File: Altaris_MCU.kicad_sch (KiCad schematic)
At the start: 82 parts, among them J1 Screw_Terminal_01x02, J10 USB_C_Receptacle_USB2.0_16P, J11 Screw_Terminal_01x02, J12 Screw_Terminal_01x02, J2 Screw_Terminal_01x02, J3 Screw_Terminal_01x02, J4 Screw_Terminal_01x02, J5 Screw_Terminal_01x02, J6 Screw_Terminal_01x02, J7 Conn_01x08_Socket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

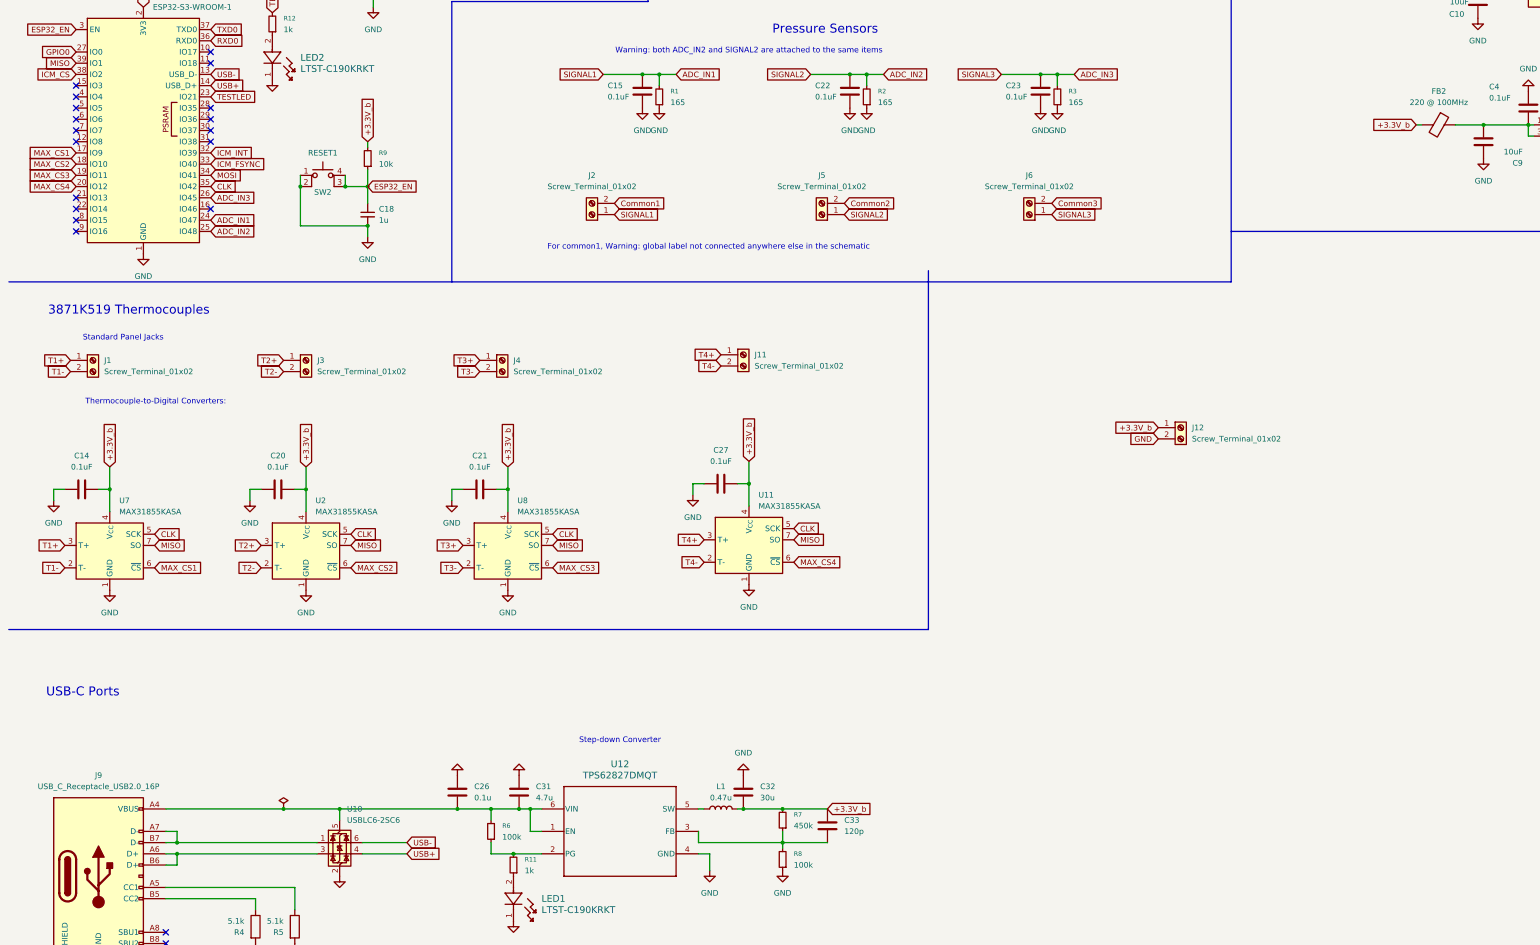
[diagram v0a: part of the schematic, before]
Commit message: added two screw terminal and MAX for extra thermocouples
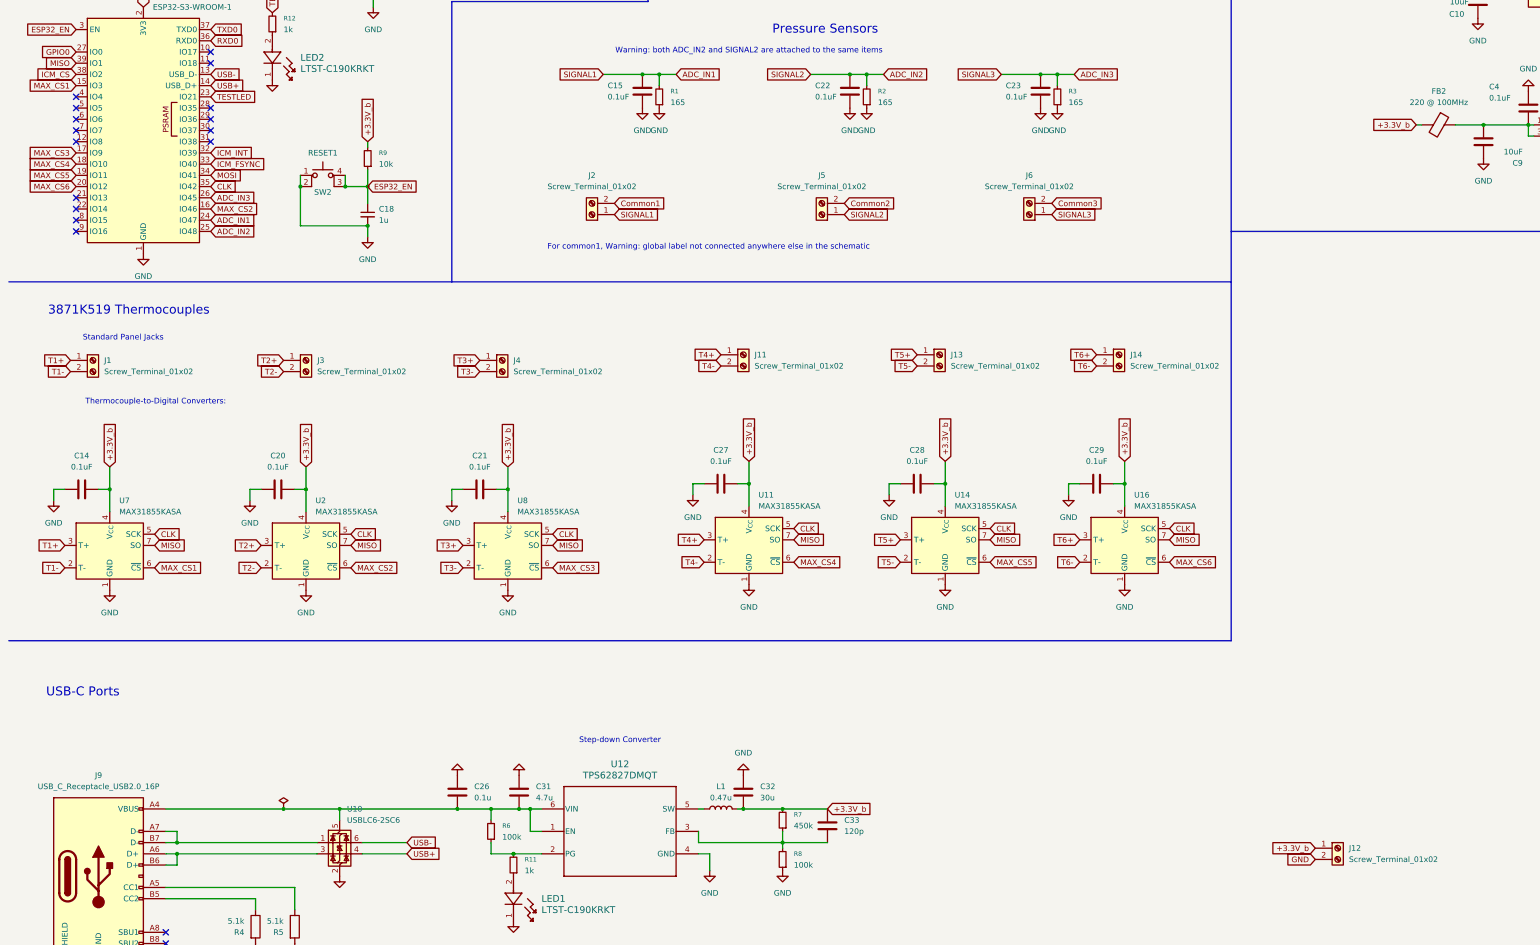
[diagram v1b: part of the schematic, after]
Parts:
- added C28, C29: 0.1uF, Capacitor_SMD:C_0402_1005Metric_Pad0.74x0.62mm_HandSolder, symbol Device:C
- added J13, J14: Screw_Terminal_01x02, TerminalBlock:TerminalBlock_MaiXu_MX126-5.0-02P_1x02_P5.00mm, symbol Connector:Screw_Terminal_01x02
- added U14, U16: MAX31855KASA, Package_SO:SOIC-8_3.9x4.9mm_P1.27mm, symbol Sensor_Temperature:MAX31855KASA
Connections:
- net +3.3V_b: now also C28.1, C29.1, U14.4 (V_{CC}), U16.4 (V_{CC})
- net CLK: now also U14.5 (SCK), U16.5 (SCK)
- net GND: now also C28.2, C29.2, U14.1 (GND), U16.1 (GND)
- net MAX_CS1: now also U1.15 (IO3); no longer U1.17 (IO9)
- net MAX_CS2: now also U1.16 (IO46); no longer U1.18 (IO10)
- net MAX_CS3: now also U1.17 (IO9); no longer U1.19 (IO11)
- net MAX_CS4: now also U1.18 (IO10); no longer U1.20 (IO12)
- net MISO: now also U14.7 (SO), U16.7 (SO)
- new net MAX_CS5: U1.19 (IO11), U14.6 (~{CS})
- new net MAX_CS6: U1.20 (IO12), U16.6 (~{CS})
- new net T5+: J13.1 (Pin_1), U14.3 (T+)
- new net T5-: J13.2 (Pin_2), U14.2 (T-)
- new net T6+: J14.1 (Pin_1), U16.3 (T+)
- new net T6-: J14.2 (Pin_2), U16.2 (T-)
- no-connect marks 30 -> 28
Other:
- moved on the sheet: J12

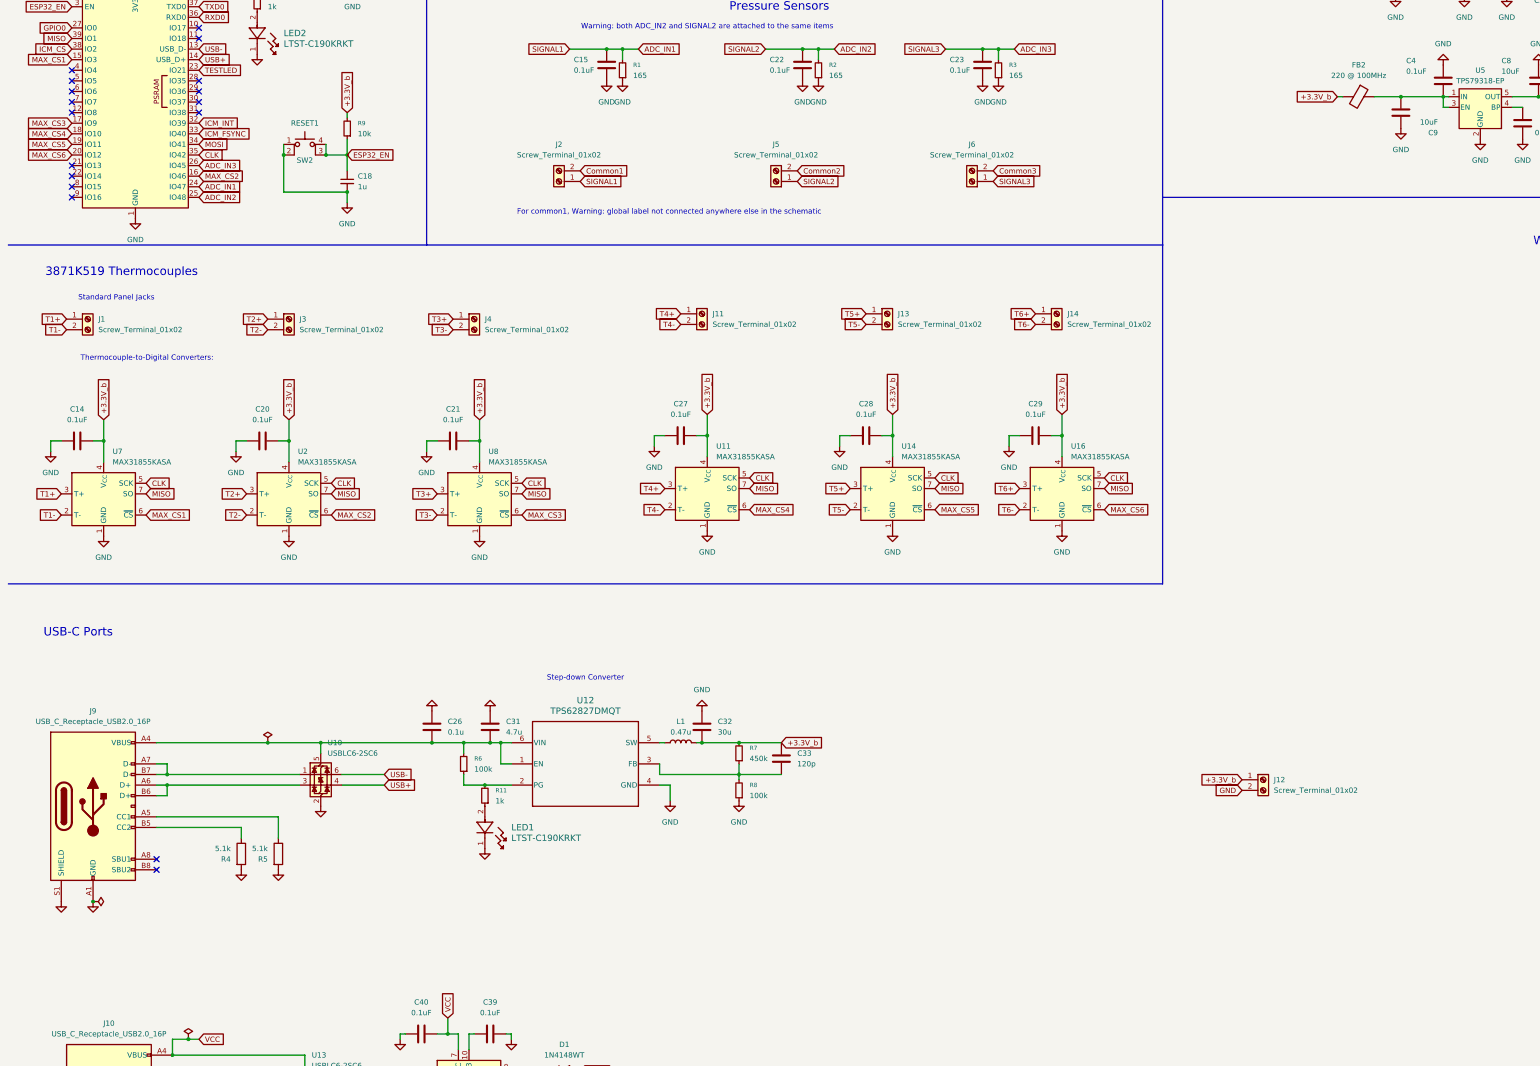
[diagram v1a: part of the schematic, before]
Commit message: Added micro SD card module w/ library
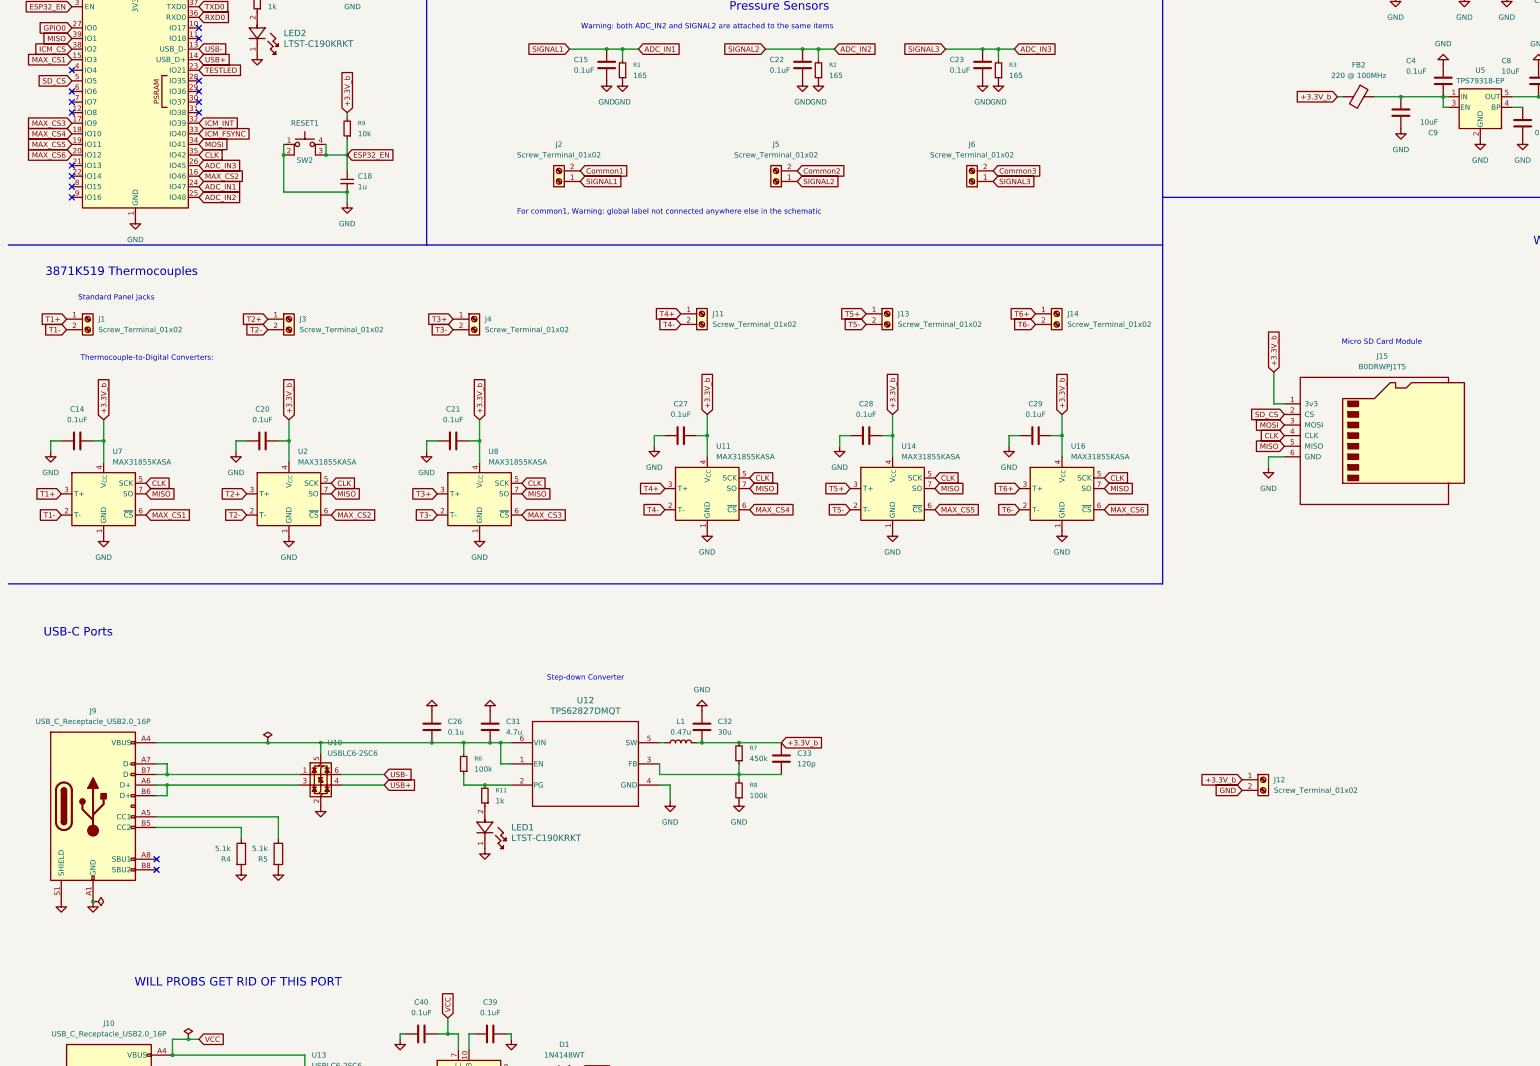
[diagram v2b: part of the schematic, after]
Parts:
- added J15: B0DRWPJ1T5, symbol Connector:Micro_SD_Card
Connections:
- net +3.3V_b: now also J15.1 (3v3)
- net CLK: now also J15.4 (CLK)
- net GND: now also J15.6 (GND)
- net MISO: now also J15.5 (MISO)
- net MOSI: now also J15.3 (MOSI)
- net SD_CS: now reaches U1.5 (IO5)
- net SD_CS: now also J15.2 (CS)
- no-connect marks 28 -> 27
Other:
- note added: "Micro SD Card Module"
- note added: "WILL PROBS GET RID OF THIS PORT"

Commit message: Added header for MicroSD module to layout, changed 3 thermocouple MAX to T type in schematic only
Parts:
- removed J15: B0DRWPJ1T5, symbol Connector:Micro_SD_Card
- removed U11, U14, U16: MAX31855KASA, Package_SO:SOIC-8_3.9x4.9mm_P1.27mm, symbol Sensor_Temperature:MAX31855KASA
- added J16: Conn_01x06, Connector_PinHeader_2.54mm:PinHeader_1x06_P2.54mm_Vertical, symbol Connector_Generic:Conn_01x06
- added U11, U17, U18: MAX31855TASA, Package_SO:SOIC-8_3.9x4.9mm_P1.27mm, symbol Sensor_Temperature:MAX31855TASA
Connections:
- net +3.3V_b: now also J16.1 (Pin_1), U11.4 (V_{CC}), U17.4 (V_{CC}), U18.4 (V_{CC})
- net CLK: now also J16.4 (Pin_4), U11.5 (SCK), U17.5 (SCK), U18.5 (SCK)
- net GND: now also J16.6 (Pin_6), U11.1 (GND), U17.1 (GND), U18.1 (GND)
- net MAX_CS4: now also U17.6 (~{CS})
- net MAX_CS5: now also U18.6 (~{CS})
- net MAX_CS6: now also U11.6 (~{CS})
- net MISO: now also J16.5 (Pin_5), U11.7 (SO), U17.7 (SO), U18.7 (SO)
- net MOSI: now also J16.3 (Pin_3)
- net SD_CS: now also J16.2 (Pin_2)
- net T4+: now also U17.3 (T+)
- net T4-: now also U17.2 (T-)
- net T5+: now also U18.3 (T+)
- net T5-: now also U18.2 (T-)
- net T6+: now also U11.3 (T+)
- net T6-: now also U11.2 (T-)

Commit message: minor edits to layout and schematic
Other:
- note added: "These have been changed to T-type in the schematic only, changes need to be updated in layout"
- note removed: "For common1, Warning: global label not connected anywhere else in the schematic"
- note removed: "Warning: both ADC_IN2 and SIGNAL2 are attached to the same items"
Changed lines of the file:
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@@
+		)
+	)
+	(text "These have been changed to T-type in the schematic only, changes need to be updated in layout\n"
+		(exclude_from_sim no)
+		(at 199.136 140.462 0)
+		(effects
+			(font
+				(size 1.27 1.27)
+			)
 		)
 	)
@@
 		)
 	)
-	(text "For common1, Warning: global label not connected anywhere else in the schematic"
-		(exclude_from_sim no)
-		(at 169.926 106.426 0)
-		(effects
-			(font
-				(size 1.27 1.27)
-			)
-		)
-	)
 	(text "Step-down Converter"
 		(exclude_from_sim no)
@@
 		(effects
 			(font
-				(size 1.27 1.27)
-			)
-		)
-	)
-	(text "Warning: both ADC_IN2 and SIGNAL2 are attached to the same items"
-		(exclude_from_sim no)
-		(at 179.07 61.976 0)
-		(effects
-			(font
